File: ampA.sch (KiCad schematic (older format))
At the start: 13 parts, among them U3 screw_term, U4 screw_term, U5 Mux, U6 MCP6004

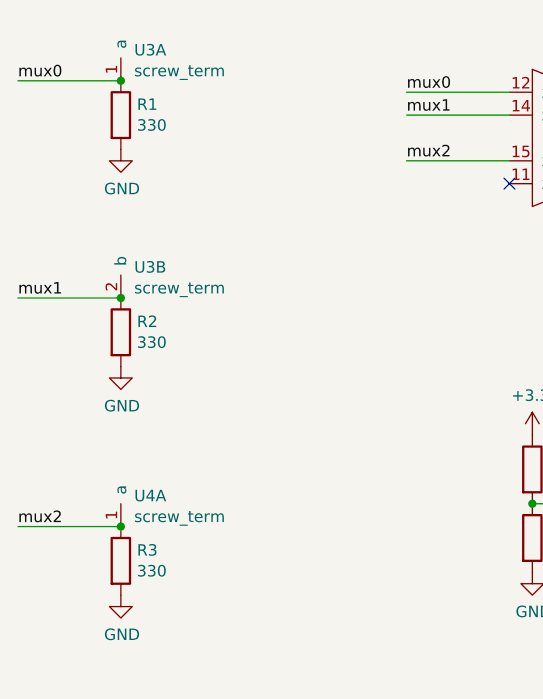
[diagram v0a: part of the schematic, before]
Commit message: added sensor sheet
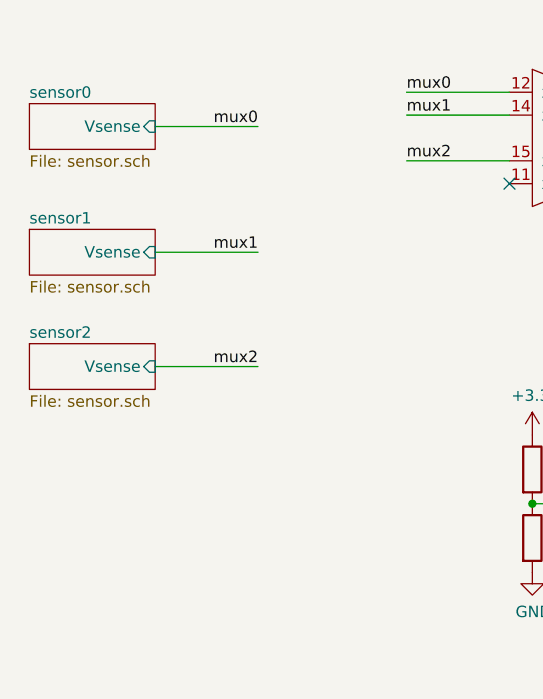
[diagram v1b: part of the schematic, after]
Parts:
- removed R1, R2, R3: 330, Resistor_THT:R_Axial_DIN0204_L3.6mm_D1.6mm_P5.08mm_Horizontal, symbol Device:R
- removed U3, U4: screw_term, Connector_PinHeader_1.27mm:PinHeader_1x02_P1.27mm_Vertical, symbol PNG_PCB_Parts:screw_term
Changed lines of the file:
@@
 $Descr A4 11693 8268
 encoding utf-8
-Sheet 2 11
+Sheet 2 14
 Title ""
 Date ""
@@
 Comment4 ""
 $EndDescr
-$Comp
-L power:GND #PWR?
-U 1 1 6013BAC9
-P 1450 2100
-AR Path="/60132BC3/6013AE22/6013BAC9" Ref="#PWR?"  Part="1"
-AR Path="/6017CC5E/6013BAC9" Ref="#PWR08"  Part="1"
-AR Path="/6017DA21/6013BAC9" Ref="#PWR?"  Part="1"
-AR Path="/601927EB/6013BAC9" Ref="#PWR?"  Part="1"
-AR Path="/6019C043/6013BAC9" Ref="#PWR?"  Part="1"
-AR Path="/601B4C0E/6013BAC9" Ref="#PWR038"  Part="1"
-AR Path="/601B73B7/6013BAC9" Ref="#PWR068"  Part="1"
-F 0 "#PWR08" H 1450 1850 50  0001 C CNN
-F 1 "GND" H 1455 1927 50  0000 C CNN
-F 2 "" H 1450 2100 50  0001 C CNN
-F 3 "" H 1450 2100 50  0001 C CNN
-	1    1450 2100
-	1    0    0    -1
-$EndComp
 $Comp
 L Device:R R?
@@
 Text HLabel 6600 3800 2    50   Input ~ 0
 out
-$Comp
-L Device:R R?
-U 1 1 6016D691
-P 1450 1950
-AR Path="/60132BC3/6013AE22/6016D691" Ref="R?"  Part="1"
-AR Path="/6017CC5E/6016D691" Ref="R1"  Part="1"
-AR Path="/6017DA21/6016D691" Ref="R?"  Part="1"
-AR Path="/601927EB/6016D691" Ref="R?"  Part="1"
-AR Path="/6019C043/6016D691" Ref="R?"  Part="1"
-AR Path="/601B4C0E/6016D691" Ref="R37"  Part="1"
-AR Path="/601B73B7/6016D691" Ref="R73"  Part="1"
-F 0 "R1" H 1520 1996 50  0000 L CNN
-F 1 "330" H 1520 1905 50  0000 L CNN
-F 2 "Resistor_THT:R_Axial_DIN0204_L3.6mm_D1.6mm_P5.08mm_Horizontal" V 1380 1950 50  0001 C CNN
-F 3 "~" H 1450 1950 50  0001 C CNN
-	1    1450 1950
-	1    0    0    -1
-$EndComp
-$Comp
-L PNG_PCB_Parts:screw_term U?
-U 1 1 6016FA62
-P 1450 1800
-AR Path="/60132BC3/6013AE22/6016FA62" Ref="U?"  Part="1"
-AR Path="/6017CC5E/6016FA62" Ref="U3"  Part="1"
-AR Path="/6017DA21/6016FA62" Ref="U?"  Part="1"
-AR Path="/601927EB/6016FA62" Ref="U?"  Part="1"
-AR Path="/6019C043/6016FA62" Ref="U?"  Part="1"
-AR Path="/601B4C0E/6016FA62" Ref="U12"  Part="1"
-AR Path="/601B73B7/6016FA62" Ref="U21"  Part="1"
-F 0 "U3" H 1508 1934 50  0000 L CNN
-F 1 "screw_term" H 1508 1843 50  0000 L CNN
-F 2 "Connector_PinHeader_1.27mm:PinHeader_1x02_P1.27mm_Vertical" H 1450 1800 50  0001 C CNN
-F 3 "" H 1450 1800 50  0001 C CNN
-	1    1450 1800
-	1    0    0    -1
-$EndComp
-Wire Wire Line
-	1450 1800 1000 1800
-Connection ~ 1450 1800
-Text Label 1000 1800 0    50   ~ 0
+Wire Wire Line
+	1600 2000 2050 2000
+Text Label 2050 2000 2    50   ~ 0
 mux0
-$Comp
-L power:GND #PWR?
-U 1 1 6019D559
-P 1450 3050
-AR Path="/60132BC3/6013AE22/6019D559" Ref="#PWR?"  Part="1"
-AR Path="/6017CC5E/6019D559" Ref="#PWR09"  Part="1"
-AR Path="/6017DA21/6019D559" Ref="#PWR?"  Part="1"
-AR Path="/601927EB/6019D559" Ref="#PWR?"  Part="1"
-AR Path="/6019C043/6019D559" Ref="#PWR?"  Part="1"
-AR Path="/601B4C0E/6019D559" Ref="#PWR039"  Part="1"
-AR Path="/601B73B7/6019D559" Ref="#PWR069"  Part="1"
-F 0 "#PWR09" H 1450 2800 50  0001 C CNN
-F 1 "GND" H 1455 2877 50  0000 C CNN
-F 2 "" H 1450 3050 50  0001 C CNN
-F 3 "" H 1450 3050 50  0001 C CNN
-	1    1450 3050
-	1    0    0    -1
-$EndComp
-$Comp
-L Device:R R?
-U 1 1 6019D56A
-P 1450 2900
-AR Path="/60132BC3/6013AE22/6019D56A" Ref="R?"  Part="1"
-AR Path="/6017CC5E/6019D56A" Ref="R2"  Part="1"
-AR Path="/6017DA21/6019D56A" Ref="R?"  Part="1"
-AR Path="/601927EB/6019D56A" Ref="R?"  Part="1"
-AR Path="/6019C043/6019D56A" Ref="R?"  Part="1"
-AR Path="/601B4C0E/6019D56A" Ref="R38"  Part="1"
-AR Path="/601B73B7/6019D56A" Ref="R74"  Part="1"
-F 0 "R2" H 1520 2946 50  0000 L CNN
-F 1 "330" H 1520 2855 50  0000 L CNN
-F 2 "Resistor_THT:R_Axial_DIN0204_L3.6mm_D1.6mm_P5.08mm_Horizontal" V 1380 2900 50  0001 C CNN
-F 3 "~" H 1450 2900 50  0001 C CNN
-	1    1450 2900
-	1    0    0    -1
-$EndComp
-$Comp
-L PNG_PCB_Parts:screw_term U?
-U 2 1 60176F25
-P 1450 2750
-AR Path="/60132BC3/6013AE22/60176F25" Ref="U?"  Part="1"
-AR Path="/6017CC5E/60176F25" Ref="U3"  Part="2"
-AR Path="/6017DA21/60176F25" Ref="U?"  Part="1"
-AR Path="/601927EB/60176F25" Ref="U?"  Part="2"
-AR Path="/6019C043/60176F25" Ref="U?"  Part="2"
-AR Path="/601B4C0E/60176F25" Ref="U12"  Part="2"
-AR Path="/601B73B7/60176F25" Ref="U21"  Part="2"
-F 0 "U3" H 1508 2884 50  0000 L CNN
-F 1 "screw_term" H 1508 2793 50  0000 L CNN
-F 2 "Connector_PinHeader_1.27mm:PinHeader_1x02_P1.27mm_Vertical" H 1450 2750 50  0001 C CNN
-F 3 "" H 1450 2750 50  0001 C CNN
-	2    1450 2750
-	1    0    0    -1
-$EndComp
-Wire Wire Line
-	1450 2750 1000 2750
-Connection ~ 1450 2750
-Text Label 1000 2750 0    50   ~ 0
-mux1
-$Comp
-L power:GND #PWR?
-U 1 1 6019D55B
-P 1450 4050
-AR Path="/60132BC3/6013AE22/6019D55B" Ref="#PWR?"  Part="1"
-AR Path="/6017CC5E/6019D55B" Ref="#PWR010"  Part="1"
-AR Path="/6017DA21/6019D55B" Ref="#PWR?"  Part="1"
-AR Path="/601927EB/6019D55B" Ref="#PWR?"  Part="1"
-AR Path="/6019C043/6019D55B" Ref="#PWR?"  Part="1"
-AR Path="/601B4C0E/6019D55B" Ref="#PWR040"  Part="1"
-AR Path="/601B73B7/6019D55B" Ref="#PWR070"  Part="1"
-F 0 "#PWR010" H 1450 3800 50  0001 C CNN
-F 1 "GND" H 1455 3877 50  0000 C CNN
-F 2 "" H 1450 4050 50  0001 C CNN
-F 3 "" H 1450 4050 50  0001 C CNN
-	1    1450 4050
-	1    0    0    -1
-$EndComp
-$Comp
-L Device:R R?
-U 1 1 6017E43F
-P 1450 3900
-AR Path="/60132BC3/6013AE22/6017E43F" Ref="R?"  Part="1"
-AR Path="/6017CC5E/6017E43F" Ref="R3"  Part="1"
-AR Path="/6017DA21/6017E43F" Ref="R?"  Part="1"
-AR Path="/601927EB/6017E43F" Ref="R?"  Part="1"
-AR Path="/6019C043/6017E43F" Ref="R?"  Part="1"
-AR Path="/601B4C0E/6017E43F" Ref="R39"  Part="1"
-AR Path="/601B73B7/6017E43F" Ref="R75"  Part="1"
-F 0 "R3" H 1520 3946 50  0000 L CNN
-F 1 "330" H 1520 3855 50  0000 L CNN
-F 2 "Resistor_THT:R_Axial_DIN0204_L3.6mm_D1.6mm_P5.08mm_Horizontal" V 1380 3900 50  0001 C CNN
-F 3 "~" H 1450 3900 50  0001 C CNN
-	1    1450 3900
-	1    0    0    -1
-$EndComp
-$Comp
-L PNG_PCB_Parts:screw_term U?
-U 1 1 6019D55C
-P 1450 3750
-AR Path="/60132BC3/6013AE22/6019D55C" Ref="U?"  Part="1"
-AR Path="/6017CC5E/6019D55C" Ref="U4"  Part="1"
-AR Path="/6017DA21/6019D55C" Ref="U?"  Part="1"
-AR Path="/601927EB/6019D55C" Ref="U?"  Part="1"
-AR Path="/6019C043/6019D55C" Ref="U?"  Part="1"
-AR Path="/601B4C0E/6019D55C" Ref="U13"  Part="1"
-AR Path="/601B73B7/6019D55C" Ref="U22"  Part="1"
-F 0 "U4" H 1508 3884 50  0000 L CNN
-F 1 "screw_term" H 1508 3793 50  0000 L CNN
-F 2 "Connector_PinHeader_1.27mm:PinHeader_1x02_P1.27mm_Vertical" H 1450 3750 50  0001 C CNN
-F 3 "" H 1450 3750 50  0001 C CNN
-	1    1450 3750
-	1    0    0    -1
-$EndComp
-Wire Wire Line
-	1450 3750 1000 3750
-Connection ~ 1450 3750
-Text Label 1000 3750 0    50   ~ 0
-mux2
 Wire Wire Line
 	3150 1850 2700 1850
@@
 	1    0    0    -1
 $EndComp
+$Sheet
+S 1050 1900 550  200
+U 60194350
+F0 "sensor0" 50
+F1 "sensor.sch" 50
+F2 "Vsense" I R 1600 2000 50
+$EndSheet
+Wire Wire Line
+	1600 2550 2050 2550
+Text Label 2050 2550 2    50   ~ 0
+mux1
+$Sheet
+S 1050 2450 550  200
+U 6019B999
+F0 "sensor1" 50
+F1 "sensor.sch" 50
+F2 "Vsense" I R 1600 2550 50
+$EndSheet
+Wire Wire Line
+	1600 3050 2050 3050
+Text Label 2050 3050 2    50   ~ 0
+mux2
+$Sheet
+S 1050 2950 550  200
+U 6019BDB6
+F0 "sensor2" 50
+F1 "sensor.sch" 50
+F2 "Vsense" I R 1600 3050 50
+$EndSheet
 $EndSCHEMATC

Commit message: switched to sensor sheet for one sensor divider
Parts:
- renumbered R4 to R1, R5 to R2, R6 to R3, R7 to R4, R8 to R5, R9 to R6, U5 to U3, U6 to U4

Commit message: updated screw terminals to 2.54mm
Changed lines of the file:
@@
 $Descr A4 11693 8268
 encoding utf-8
-Sheet 2 41
+Sheet 18 41
 Title ""
 Date ""
@@
 AR Path="/601B4C0E/6019D565" Ref="R65"  Part="1"
 AR Path="/601B73B7/6019D565" Ref="R125"  Part="1"
-F 0 "R125" H 5520 4096 50  0000 L CNN
+F 0 "R65" H 5520 4096 50  0000 L CNN
 F 1 "15" H 5520 4005 50  0000 L CNN
 F 2 "Resistor_THT:R_Axial_DIN0204_L3.6mm_D1.6mm_P5.08mm_Horizontal" V 5380 4050 50  0001 C CNN
@@
 AR Path="/601B4C0E/60198F32" Ref="R66"  Part="1"
 AR Path="/601B73B7/60198F32" Ref="R126"  Part="1"
-F 0 "R126" V 5743 3250 50  0000 C CNN
+F 0 "R66" V 5743 3250 50  0000 C CNN
 F 1 "15" V 5834 3250 50  0000 C CNN
 F 2 "Resistor_THT:R_Axial_DIN0204_L3.6mm_D1.6mm_P5.08mm_Horizontal" V 5880 3250 50  0001 C CNN
@@
 AR Path="/601B4C0E/6017E431" Ref="R63"  Part="1"
 AR Path="/601B73B7/6017E431" Ref="R123"  Part="1"
-F 0 "R123" V 5307 3700 50  0000 C CNN
+F 0 "R63" V 5307 3700 50  0000 C CNN
 F 1 "1" V 5216 3700 50  0000 C CNN
 F 2 "Resistor_THT:R_Axial_DIN0204_L3.6mm_D1.6mm_P5.08mm_Horizontal" V 5030 3700 50  0001 C CNN
@@
 AR Path="/601B4C0E/6019D568" Ref="R64"  Part="1"
 AR Path="/601B73B7/6019D568" Ref="R124"  Part="1"
-F 0 "R124" V 5000 3900 50  0000 C CNN
+F 0 "R64" V 5000 3900 50  0000 C CNN
 F 1 "1" V 4900 3900 50  0000 C CNN
 F 2 "Resistor_THT:R_Axial_DIN0204_L3.6mm_D1.6mm_P5.08mm_Horizontal" V 5030 3900 50  0001 C CNN
@@
 AR Path="/601B4C0E/6019D55E" Ref="R61"  Part="1"
 AR Path="/601B73B7/6019D55E" Ref="R121"  Part="1"
-F 0 "R121" H 3320 3546 50  0000 L CNN
+F 0 "R61" H 3320 3546 50  0000 L CNN
 F 1 "330" H 3320 3455 50  0000 L CNN
 F 2 "Resistor_THT:R_Axial_DIN0204_L3.6mm_D1.6mm_P5.08mm_Horizontal" V 3180 3500 50  0001 C CNN
@@
 AR Path="/601B4C0E/6019D55F" Ref="R62"  Part="1"
 AR Path="/601B73B7/6019D55F" Ref="R122"  Part="1"
-F 0 "R122" H 3320 3846 50  0000 L CNN
+F 0 "R62" H 3320 3846 50  0000 L CNN
 F 1 "560" H 3320 3755 50  0000 L CNN
 F 2 "Resistor_THT:R_Axial_DIN0204_L3.6mm_D1.6mm_P5.08mm_Horizontal" V 3180 3800 50  0001 C CNN
@@
 AR Path="/601B4C0E/6019D560" Ref="#PWR098"  Part="1"
 AR Path="/601B73B7/6019D560" Ref="#PWR0188"  Part="1"
-F 0 "#PWR0188" H 3250 3200 50  0001 C CNN
+F 0 "#PWR098" H 3250 3200 50  0001 C CNN
 F 1 "+3.3V" H 3265 3523 50  0000 C CNN
 F 2 "" H 3250 3350 50  0001 C CNN
@@
 AR Path="/601B4C0E/60198F38" Ref="#PWR099"  Part="1"
 AR Path="/601B73B7/60198F38" Ref="#PWR0189"  Part="1"
-F 0 "#PWR0189" H 3250 3700 50  0001 C CNN
+F 0 "#PWR099" H 3250 3700 50  0001 C CNN
 F 1 "GND" H 3255 3777 50  0000 C CNN
 F 2 "" H 3250 3950 50  0001 C CNN
@@
 AR Path="/601B4C0E/6016B854" Ref="#PWR0100"  Part="1"
 AR Path="/601B73B7/6016B854" Ref="#PWR0190"  Part="1"
-F 0 "#PWR0190" H 5450 3950 50  0001 C CNN
+F 0 "#PWR0100" H 5450 3950 50  0001 C CNN
 F 1 "GND" H 5455 4027 50  0000 C CNN
 F 2 "" H 5450 4200 50  0001 C CNN
@@
 AR Path="/601B4C0E/601899DD" Ref="#PWR0102"  Part="1"
 AR Path="/601B73B7/601899DD" Ref="#PWR0192"  Part="1"
-F 0 "#PWR0192" H 5700 2050 50  0001 C CNN
+F 0 "#PWR0102" H 5700 2050 50  0001 C CNN
 F 1 "GND" H 5705 2127 50  0000 C CNN
 F 2 "" H 5700 2300 50  0001 C CNN
@@
 AR Path="/601B4C0E/60189E9E" Ref="#PWR0101"  Part="1"
 AR Path="/601B73B7/60189E9E" Ref="#PWR0191"  Part="1"
-F 0 "#PWR0191" H 5700 1600 50  0001 C CNN
+F 0 "#PWR0101" H 5700 1600 50  0001 C CNN
 F 1 "+3.3V" H 5715 1923 50  0000 C CNN
 F 2 "" H 5700 1750 50  0001 C CNN
@@
 AR Path="/601B4C0E/60195FF1" Ref="#PWR0104"  Part="1"
 AR Path="/601B73B7/60195FF1" Ref="#PWR0194"  Part="1"
-F 0 "#PWR0194" H 7150 2100 50  0001 C CNN
+F 0 "#PWR0104" H 7150 2100 50  0001 C CNN
 F 1 "GND" H 7155 2177 50  0000 C CNN
 F 2 "" H 7150 2350 50  0001 C CNN
@@
 AR Path="/601B4C0E/60198969" Ref="#PWR0103"  Part="1"
 AR Path="/601B73B7/60198969" Ref="#PWR0193"  Part="1"
-F 0 "#PWR0193" H 7150 1600 50  0001 C CNN
+F 0 "#PWR0103" H 7150 1600 50  0001 C CNN
 F 1 "+3.3V" H 7165 1923 50  0000 C CNN
 F 2 "" H 7150 1750 50  0001 C CNN
@@
 AR Path="/601B4C0E/6016DEDC" Ref="U6"  Part="1"
 AR Path="/601B73B7/6016DEDC" Ref="U9"  Part="1"
-F 0 "U9" H 3375 2515 50  0000 C CNN
+F 0 "U6" H 3375 2515 50  0000 C CNN
 F 1 "Mux" H 3375 2424 50  0000 C CNN
 F 2 "Package_DIP:DIP-16_W7.62mm" H 3350 2050 50  0001 C CNN
@@
 AR Path="/601B4C0E/6016F806" Ref="U6"  Part="3"
 AR Path="/601B73B7/6016F806" Ref="U9"  Part="3"
-F 0 "U9" H 5928 2221 50  0000 L CNN
+F 0 "U6" H 5928 2221 50  0000 L CNN
 F 1 "Mux" H 5928 2130 50  0000 L CNN
 F 2 "Package_DIP:DIP-16_W7.62mm" H 5700 2100 50  0001 C CNN
@@
 AR Path="/601B4C0E/60189002" Ref="U7"  Part="1"
 AR Path="/601B73B7/60189002" Ref="U10"  Part="1"
-F 0 "U10" H 6000 4167 50  0000 C CNN
+F 0 "U7" H 6000 4167 50  0000 C CNN
 F 1 "MCP6004" H 6000 4076 50  0000 C CNN
 F 2 "Package_DIP:DIP-14_W7.62mm" H 5950 3900 50  0001 C CNN
@@
 AR Path="/601B4C0E/6018B5B8" Ref="U7"  Part="5"
 AR Path="/601B73B7/6018B5B8" Ref="U10"  Part="5"
-F 0 "U10" H 7208 2096 50  0000 L CNN
+F 0 "U7" H 7208 2096 50  0000 L CNN
 F 1 "MCP6004" H 7208 2005 50  0000 L CNN
 F 2 "Package_DIP:DIP-14_W7.62mm" H 7200 2150 50  0001 C CNN

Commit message: removed stacked components
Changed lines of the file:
@@
 $Descr A4 11693 8268
 encoding utf-8
-Sheet 18 41
+Sheet 2 41
 Title ""
 Date ""
@@
 AR Path="/601B4C0E/6019D565" Ref="R65"  Part="1"
 AR Path="/601B73B7/6019D565" Ref="R125"  Part="1"
-F 0 "R65" H 5520 4096 50  0000 L CNN
+F 0 "R5" H 5520 4096 50  0000 L CNN
 F 1 "15" H 5520 4005 50  0000 L CNN
 F 2 "Resistor_THT:R_Axial_DIN0204_L3.6mm_D1.6mm_P5.08mm_Horizontal" V 5380 4050 50  0001 C CNN
@@
 AR Path="/601B4C0E/60198F32" Ref="R66"  Part="1"
 AR Path="/601B73B7/60198F32" Ref="R126"  Part="1"
-F 0 "R66" V 5743 3250 50  0000 C CNN
+F 0 "R6" V 5743 3250 50  0000 C CNN
 F 1 "15" V 5834 3250 50  0000 C CNN
 F 2 "Resistor_THT:R_Axial_DIN0204_L3.6mm_D1.6mm_P5.08mm_Horizontal" V 5880 3250 50  0001 C CNN
@@
 AR Path="/601B4C0E/6017E431" Ref="R63"  Part="1"
 AR Path="/601B73B7/6017E431" Ref="R123"  Part="1"
-F 0 "R63" V 5307 3700 50  0000 C CNN
+F 0 "R3" V 5307 3700 50  0000 C CNN
 F 1 "1" V 5216 3700 50  0000 C CNN
 F 2 "Resistor_THT:R_Axial_DIN0204_L3.6mm_D1.6mm_P5.08mm_Horizontal" V 5030 3700 50  0001 C CNN
@@
 AR Path="/601B4C0E/6019D568" Ref="R64"  Part="1"
 AR Path="/601B73B7/6019D568" Ref="R124"  Part="1"
-F 0 "R64" V 5000 3900 50  0000 C CNN
+F 0 "R4" V 5000 3900 50  0000 C CNN
 F 1 "1" V 4900 3900 50  0000 C CNN
 F 2 "Resistor_THT:R_Axial_DIN0204_L3.6mm_D1.6mm_P5.08mm_Horizontal" V 5030 3900 50  0001 C CNN
@@
 AR Path="/601B4C0E/6019D55E" Ref="R61"  Part="1"
 AR Path="/601B73B7/6019D55E" Ref="R121"  Part="1"
-F 0 "R61" H 3320 3546 50  0000 L CNN
+F 0 "R1" H 3320 3546 50  0000 L CNN
 F 1 "330" H 3320 3455 50  0000 L CNN
 F 2 "Resistor_THT:R_Axial_DIN0204_L3.6mm_D1.6mm_P5.08mm_Horizontal" V 3180 3500 50  0001 C CNN
@@
 AR Path="/601B4C0E/6019D55F" Ref="R62"  Part="1"
 AR Path="/601B73B7/6019D55F" Ref="R122"  Part="1"
-F 0 "R62" H 3320 3846 50  0000 L CNN
+F 0 "R2" H 3320 3846 50  0000 L CNN
 F 1 "560" H 3320 3755 50  0000 L CNN
 F 2 "Resistor_THT:R_Axial_DIN0204_L3.6mm_D1.6mm_P5.08mm_Horizontal" V 3180 3800 50  0001 C CNN
@@
 AR Path="/601B4C0E/6019D560" Ref="#PWR098"  Part="1"
 AR Path="/601B73B7/6019D560" Ref="#PWR0188"  Part="1"
-F 0 "#PWR098" H 3250 3200 50  0001 C CNN
+F 0 "#PWR0188" H 3250 3200 50  0001 C CNN
 F 1 "+3.3V" H 3265 3523 50  0000 C CNN
 F 2 "" H 3250 3350 50  0001 C CNN
@@
 AR Path="/601B4C0E/60198F38" Ref="#PWR099"  Part="1"
 AR Path="/601B73B7/60198F38" Ref="#PWR0189"  Part="1"
-F 0 "#PWR099" H 3250 3700 50  0001 C CNN
+F 0 "#PWR0189" H 3250 3700 50  0001 C CNN
 F 1 "GND" H 3255 3777 50  0000 C CNN
 F 2 "" H 3250 3950 50  0001 C CNN
@@
 AR Path="/601B4C0E/6016B854" Ref="#PWR0100"  Part="1"
 AR Path="/601B73B7/6016B854" Ref="#PWR0190"  Part="1"
-F 0 "#PWR0100" H 5450 3950 50  0001 C CNN
+F 0 "#PWR0190" H 5450 3950 50  0001 C CNN
 F 1 "GND" H 5455 4027 50  0000 C CNN
 F 2 "" H 5450 4200 50  0001 C CNN
@@
 AR Path="/601B4C0E/601899DD" Ref="#PWR0102"  Part="1"
 AR Path="/601B73B7/601899DD" Ref="#PWR0192"  Part="1"
-F 0 "#PWR0102" H 5700 2050 50  0001 C CNN
+F 0 "#PWR0192" H 5700 2050 50  0001 C CNN
 F 1 "GND" H 5705 2127 50  0000 C CNN
 F 2 "" H 5700 2300 50  0001 C CNN
@@
 AR Path="/601B4C0E/60189E9E" Ref="#PWR0101"  Part="1"
 AR Path="/601B73B7/60189E9E" Ref="#PWR0191"  Part="1"
-F 0 "#PWR0101" H 5700 1600 50  0001 C CNN
+F 0 "#PWR0191" H 5700 1600 50  0001 C CNN
 F 1 "+3.3V" H 5715 1923 50  0000 C CNN
 F 2 "" H 5700 1750 50  0001 C CNN
@@
 AR Path="/601B4C0E/60195FF1" Ref="#PWR0104"  Part="1"
 AR Path="/601B73B7/60195FF1" Ref="#PWR0194"  Part="1"
-F 0 "#PWR0104" H 7150 2100 50  0001 C CNN
+F 0 "#PWR0194" H 7150 2100 50  0001 C CNN
 F 1 "GND" H 7155 2177 50  0000 C CNN
 F 2 "" H 7150 2350 50  0001 C CNN
@@
 AR Path="/601B4C0E/60198969" Ref="#PWR0103"  Part="1"
 AR Path="/601B73B7/60198969" Ref="#PWR0193"  Part="1"
-F 0 "#PWR0103" H 7150 1600 50  0001 C CNN
+F 0 "#PWR0193" H 7150 1600 50  0001 C CNN
 F 1 "+3.3V" H 7165 1923 50  0000 C CNN
 F 2 "" H 7150 1750 50  0001 C CNN
@@
 AR Path="/601B4C0E/6016DEDC" Ref="U6"  Part="1"
 AR Path="/601B73B7/6016DEDC" Ref="U9"  Part="1"
-F 0 "U6" H 3375 2515 50  0000 C CNN
+F 0 "U3" H 3375 2515 50  0000 C CNN
 F 1 "Mux" H 3375 2424 50  0000 C CNN
 F 2 "Package_DIP:DIP-16_W7.62mm" H 3350 2050 50  0001 C CNN
@@
 AR Path="/601B4C0E/6016F806" Ref="U6"  Part="3"
 AR Path="/601B73B7/6016F806" Ref="U9"  Part="3"
-F 0 "U6" H 5928 2221 50  0000 L CNN
+F 0 "U3" H 5928 2221 50  0000 L CNN
 F 1 "Mux" H 5928 2130 50  0000 L CNN
 F 2 "Package_DIP:DIP-16_W7.62mm" H 5700 2100 50  0001 C CNN
@@
 AR Path="/601B4C0E/60189002" Ref="U7"  Part="1"
 AR Path="/601B73B7/60189002" Ref="U10"  Part="1"
-F 0 "U7" H 6000 4167 50  0000 C CNN
+F 0 "U4" H 6000 4167 50  0000 C CNN
 F 1 "MCP6004" H 6000 4076 50  0000 C CNN
 F 2 "Package_DIP:DIP-14_W7.62mm" H 5950 3900 50  0001 C CNN
@@
 AR Path="/601B4C0E/6018B5B8" Ref="U7"  Part="5"
 AR Path="/601B73B7/6018B5B8" Ref="U10"  Part="5"
-F 0 "U7" H 7208 2096 50  0000 L CNN
+F 0 "U4" H 7208 2096 50  0000 L CNN
 F 1 "MCP6004" H 7208 2005 50  0000 L CNN
 F 2 "Package_DIP:DIP-14_W7.62mm" H 7200 2150 50  0001 C CNN
